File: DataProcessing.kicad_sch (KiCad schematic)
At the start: 9 parts, among them J3 AVR-ISP-6, U2 ATmega328PB-M

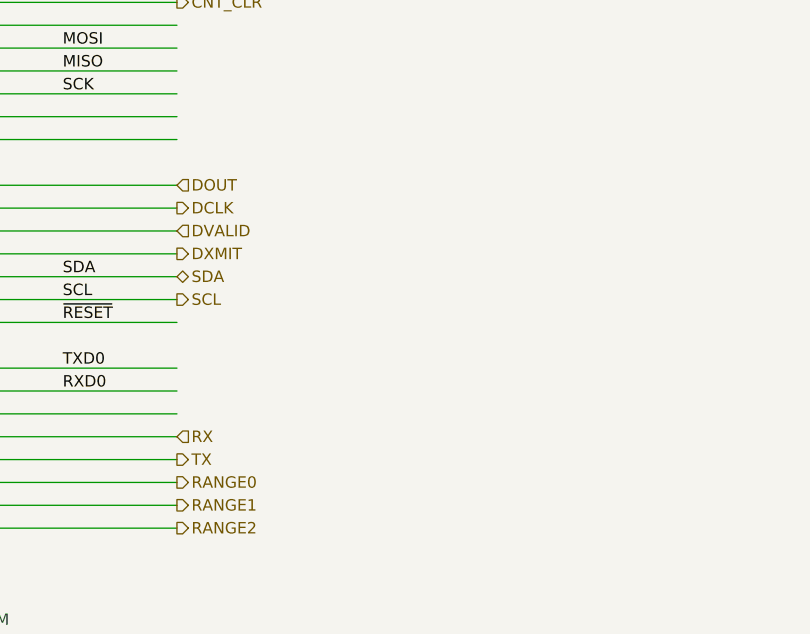
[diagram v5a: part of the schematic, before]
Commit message: implemented I2C incl. pullups
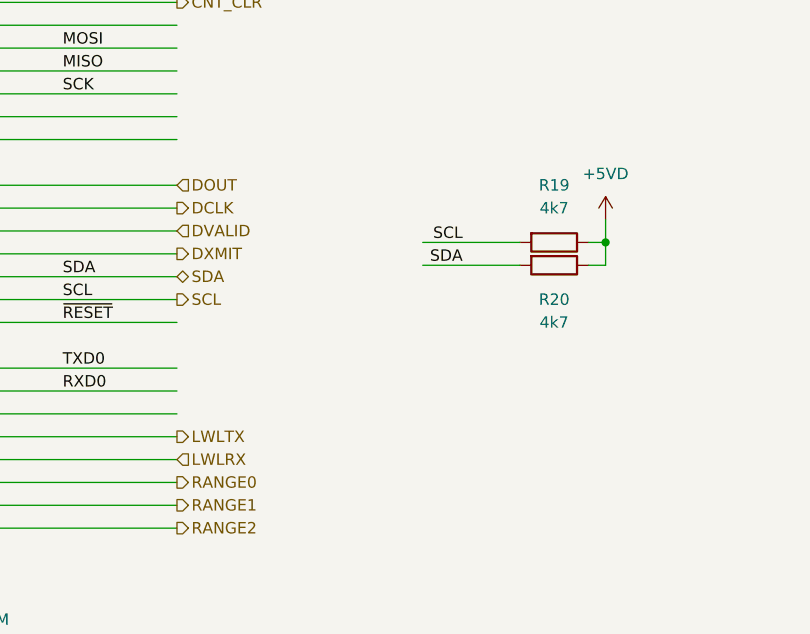
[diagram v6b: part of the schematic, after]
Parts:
- added R19, R20: 4k7, Resistor_SMD:R_0603_1608Metric, symbol Device:R
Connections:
- net +5VD: now also R19.1, R20.1
- net SCL: now also R19.2
- net SDA: now also R20.2
- net RX renamed LWLTX
- net TX renamed LWLRX
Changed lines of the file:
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@@
   (junction (at 92.71 53.34) (diameter 0) (color 0 0 0 0)
   )
+  (junction (at 174.625 92.71) (diameter 0) (color 0 0 0 0)
+  )
   (wire (pts (xy 121.92 40.64) (xy 121.92 41.91))
     (stroke (width 0) (type default) (color 0 0 0 0))
@@
     (stroke (width 0) (type default) (color 0 0 0 0))
   )
+  (wire (pts (xy 154.305 95.25) (xy 165.1 95.25))
+    (stroke (width 0) (type default) (color 0 0 0 0))
+  )
   (wire (pts (xy 91.44 132.08) (xy 91.44 139.7))
     (stroke (width 0) (type default) (color 0 0 0 0))
@@
     (stroke (width 0) (type default) (color 0 0 0 0))
   )
+  (wire (pts (xy 172.72 95.25) (xy 174.625 95.25))
+    (stroke (width 0) (type default) (color 0 0 0 0))
+  )
   (wire (pts (xy 39.37 87.63) (xy 39.37 91.44))
     (stroke (width 0) (type default) (color 0 0 0 0))
@@
     (stroke (width 0) (type default) (color 0 0 0 0))
   )
+  (wire (pts (xy 172.72 92.71) (xy 174.625 92.71))
+    (stroke (width 0) (type default) (color 0 0 0 0))
+  )
   (wire (pts (xy 72.39 106.68) (xy 76.2 106.68))
     (stroke (width 0) (type default) (color 0 0 0 0))
@@
     (stroke (width 0) (type default) (color 0 0 0 0))
   )
+  (wire (pts (xy 154.305 92.71) (xy 165.1 92.71))
+    (stroke (width 0) (type default) (color 0 0 0 0))
+  )
   (wire (pts (xy 91.44 53.34) (xy 92.71 53.34))
     (stroke (width 0) (type default) (color 0 0 0 0))
@@
     (stroke (width 0) (type default) (color 0 0 0 0))
   )
+  (wire (pts (xy 174.625 90.17) (xy 174.625 92.71))
+    (stroke (width 0) (type default) (color 0 0 0 0))
+  )
   (wire (pts (xy 212.09 50.8) (xy 219.71 50.8))
     (stroke (width 0) (type default) (color 0 0 0 0))
@@
     (stroke (width 0) (type default) (color 0 0 0 0))
   )
+  (wire (pts (xy 174.625 95.25) (xy 174.625 92.71))
+    (stroke (width 0) (type default) (color 0 0 0 0))
+  )
   (text "Digitize data and send to interface part via UART" (at 182.88 171.45 0)
     (effects (font (size 1.27 1.27)) (justify left bottom))
@@
     (effects (font (size 1.27 1.27)) (justify left bottom))
   )
+  (label "SCL" (at 158.75 92.71 180)
+    (effects (font (size 1.27 1.27)) (justify right bottom))
+  )
   (label "MISO" (at 114.3 73.66 0)
     (effects (font (size 1.27 1.27)) (justify left bottom))
   )
+  (label "SDA" (at 158.75 95.25 180)
+    (effects (font (size 1.27 1.27)) (justify right bottom))
+  )
   (label "TXD0" (at 114.3 106.68 0)
     (effects (font (size 1.27 1.27)) (justify left bottom))
@@
   )
   (hierarchical_label "DOUT" (shape input) (at 127 86.36 0)
-    (effects (font (size 1.27 1.27)) (justify left))
-  )
-  (hierarchical_label "RX" (shape input) (at 127 114.3 0)
     (effects (font (size 1.27 1.27)) (justify left))
   )
@@
     (effects (font (size 1.27 1.27)) (justify right))
   )
-  (hierarchical_label "TX" (shape output) (at 127 116.84 0)
+  (hierarchical_label "LWLRX" (shape input) (at 127 116.84 0)
     (effects (font (size 1.27 1.27)) (justify left))
   )
@@
   )
   (hierarchical_label "DCLK" (shape output) (at 127 88.9 0)
+    (effects (font (size 1.27 1.27)) (justify left))
+  )
+  (hierarchical_label "LWLTX" (shape output) (at 127 114.3 0)
     (effects (font (size 1.27 1.27)) (justify left))
   )
@@
     (pin "1")
   )
+  (symbol (lib_id "Device:R") (at 168.91 92.71 270) (unit 1)
+    (in_bom yes) (on_board yes) (fields_autoplaced)
+    (property "Reference" "R19" (id 0) (at 168.91 86.36 90))
+    (property "Value" "4k7" (id 1) (at 168.91 88.9 90))
+    (property "Footprint" "Resistor_SMD:R_0603_1608Metric" (id 2) (at 168.91 90.932 90)
+      (effects (font (size 1.27 1.27)) hide)
+    )
+    (property "Datasheet" "~" (id 3) (at 168.91 92.71 0)
+      (effects (font (size 1.27 1.27)) hide)
+    )
+    (pin "1")
+    (pin "2")
+  )
   (symbol (lib_id "Device:C") (at 133.35 36.83 0) (unit 1)
     (in_bom yes) (on_board yes) (fields_autoplaced)
@@
     )
     (property "Datasheet" "" (id 3) (at 133.35 31.75 0)
+      (effects (font (size 1.27 1.27)) hide)
+    )
+    (pin "1")
+  )
+  (symbol (lib_id "power:+5VD") (at 174.625 90.17 0) (unit 1)
+    (in_bom yes) (on_board yes) (fields_autoplaced)
+    (property "Reference" "#PWR042" (id 0) (at 174.625 93.98 0)
+      (effects (font (size 1.27 1.27)) hide)
+    )
+    (property "Value" "+5VD" (id 1) (at 174.625 85.09 0))
+    (property "Footprint" "" (id 2) (at 174.625 90.17 0)
+      (effects (font (size 1.27 1.27)) hide)
+    )
+    (property "Datasheet" "" (id 3) (at 174.625 90.17 0)
       (effects (font (size 1.27 1.27)) hide)
     )
@@
     (pin "1")
   )
+  (symbol (lib_id "Device:R") (at 168.91 95.25 270) (unit 1)
+    (in_bom yes) (on_board yes) (fields_autoplaced)
+    (property "Reference" "R20" (id 0) (at 168.91 99.06 90))
+    (property "Value" "4k7" (id 1) (at 168.91 101.6 90))
+    (property "Footprint" "Resistor_SMD:R_0603_1608Metric" (id 2) (at 168.91 93.472 90)
+      (effects (font (size 1.27 1.27)) hide)
+    )
+    (property "Datasheet" "~" (id 3) (at 168.91 95.25 0)
+      (effects (font (size 1.27 1.27)) hide)
+    )
+    (pin "1")
+    (pin "2")
+  )
 )
